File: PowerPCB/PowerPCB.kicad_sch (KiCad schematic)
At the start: 68 parts, among them J4 Conn_01x03, J5 Conn_01x02, J6 Conn_01x02, U1 TPS551892QWRYQRQ1, U2 FS1003-0600-AL, U4 TPS551892QWRYQRQ1

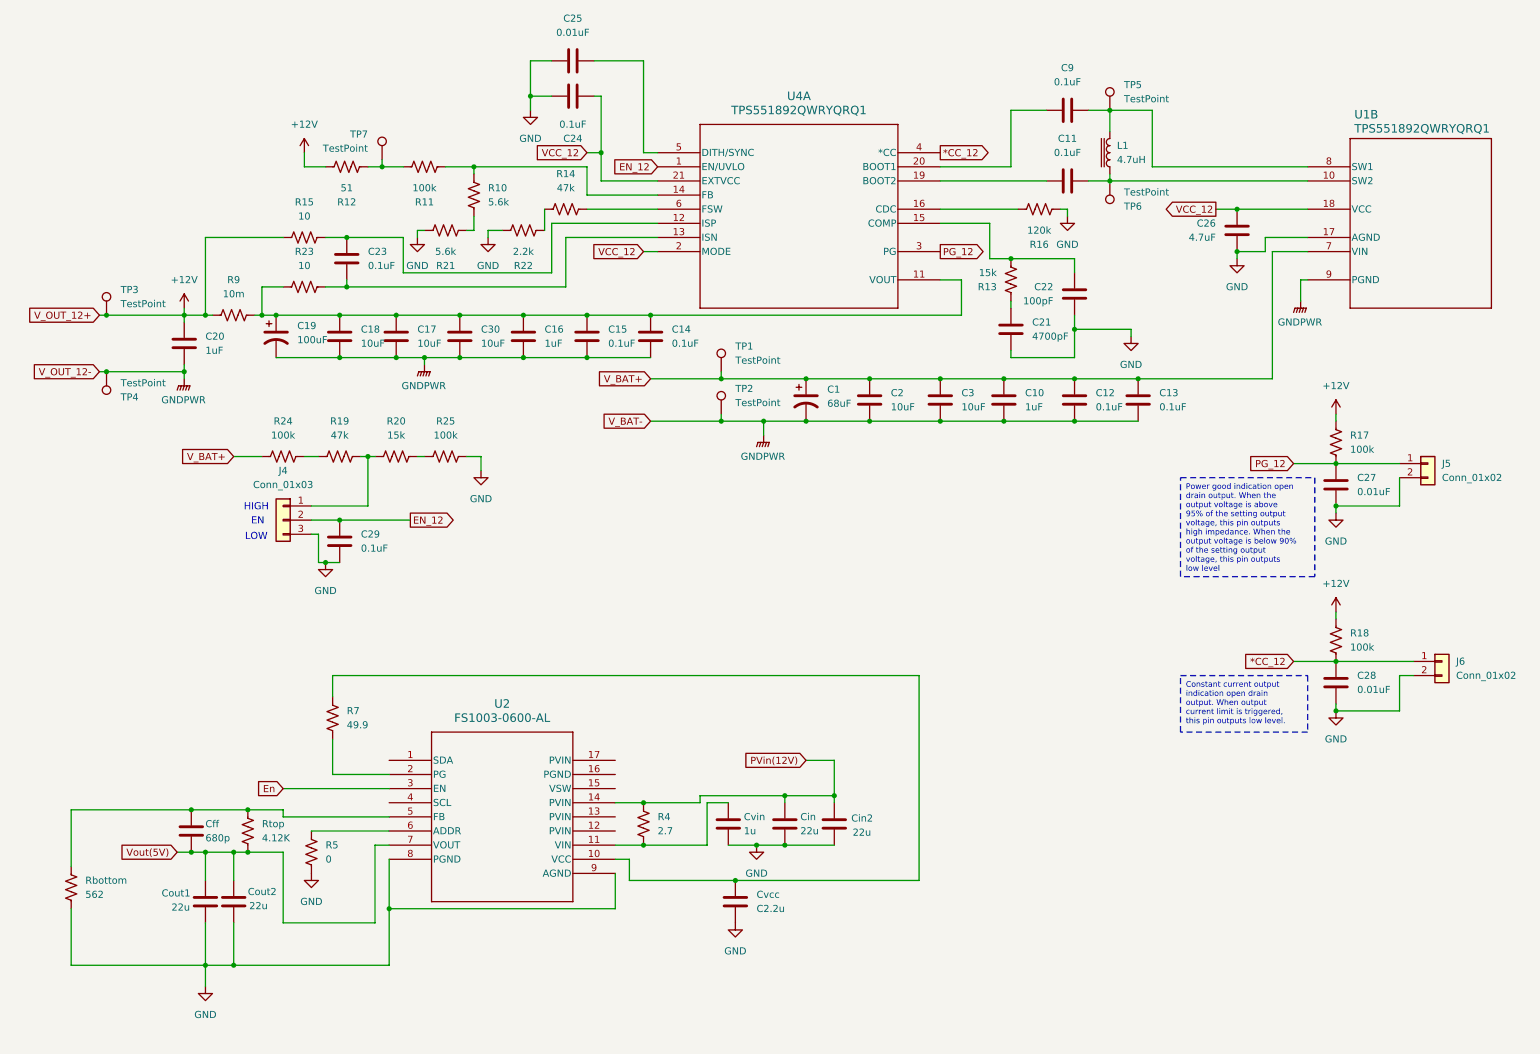
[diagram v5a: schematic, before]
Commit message: Change FS1003 to FS1403
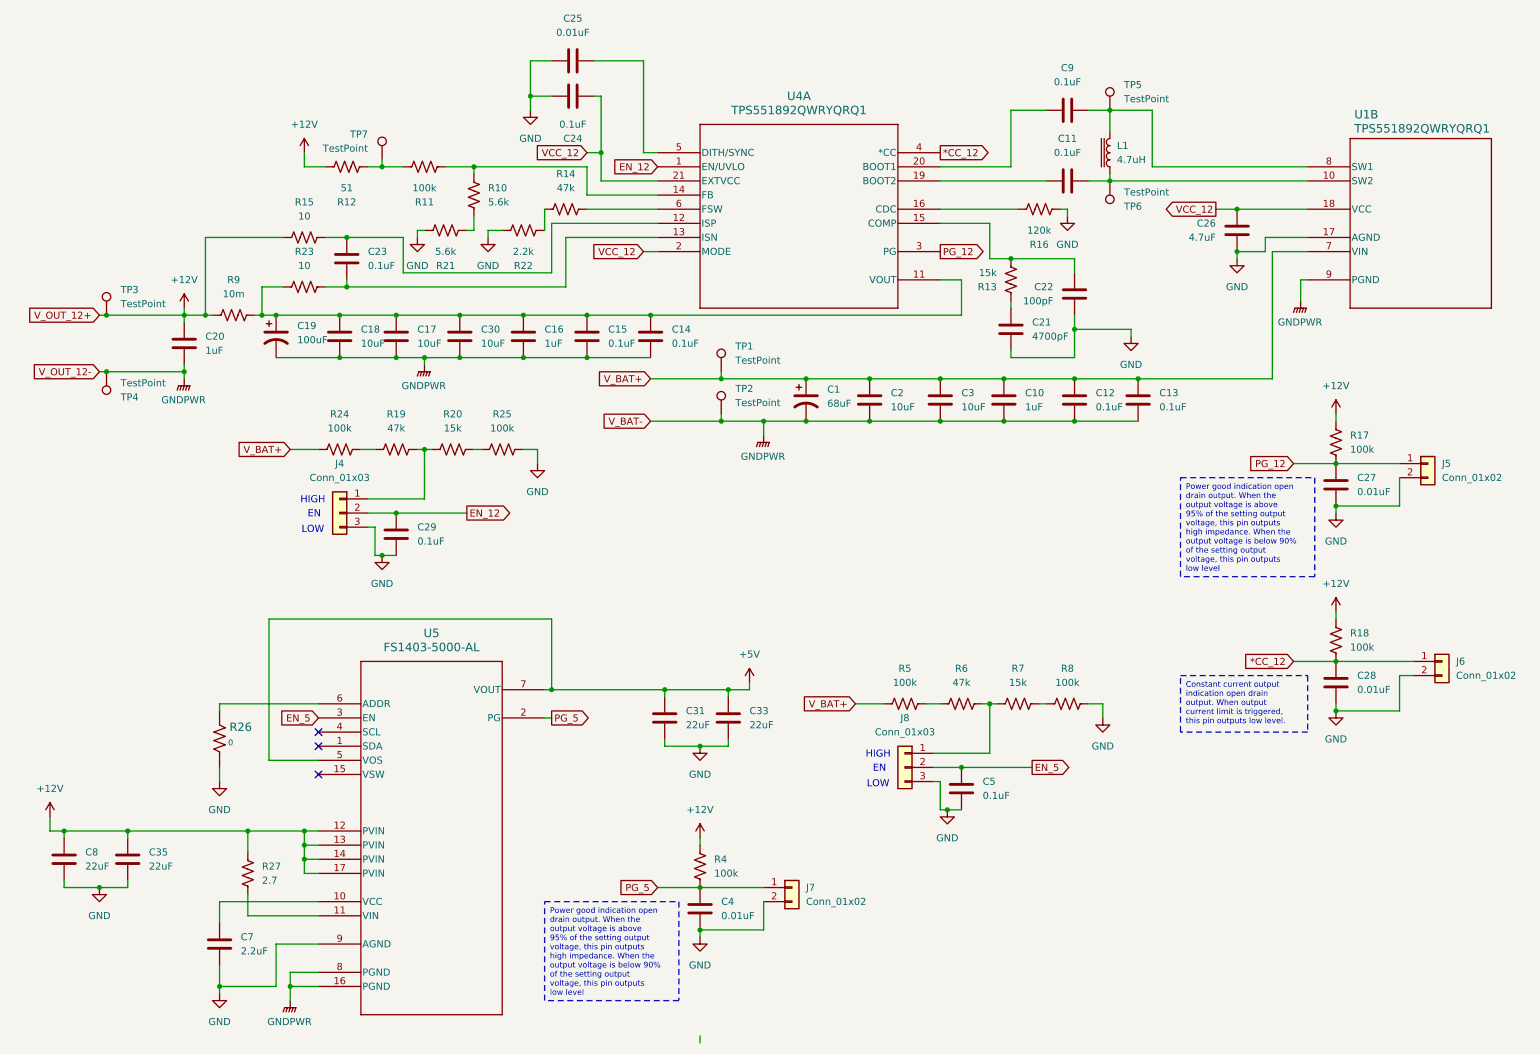
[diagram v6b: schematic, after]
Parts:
- removed Cff: 680p, symbol Device:C
- removed Cin, Cin2, Cout1, Cout2: 22u, symbol Device:C
- removed Cvcc: C2.2u, symbol Device:C
- removed Cvin: 1u, symbol Device:C
- removed Rbottom: 562, symbol Device:R_US
- removed Rtop: 4.12K, symbol Device:R_US
- removed U2: FS1003-0600-AL, Kicad_TitoSync_Footprints:fs1003-0600-al, symbol KiCad_TitoSync_Symbols:FS1003-0600-AL
- added C31, C33, C35, C8: 22uF, symbol Device:C
- added C4: 0.01uF, Capacitor_SMD:C_0805_2012Metric_Pad1.18x1.45mm_HandSolder, symbol Device:C
- added C5: 0.1uF, Capacitor_SMD:C_1206_3216Metric_Pad1.33x1.80mm_HandSolder, symbol Device:C
- added C7: 2.2uF, symbol Device:C
- added J7: Conn_01x02, Connector_PinHeader_2.54mm:PinHeader_1x02_P2.54mm_Vertical, symbol Connector_Generic:Conn_01x02
- added J8: Conn_01x03, Connector_PinHeader_2.54mm:PinHeader_1x03_P2.54mm_Vertical, symbol Connector_Generic:Conn_01x03
- added R26: 0, POWER STRIP DESIGN WITH ORIGINAL:0402, symbol POWER_STRIP_DESIGN_WITH_ORIGINAL-lib:R
- added R27: 2.7, symbol Device:R_US
- added R6: 47k, Resistor_SMD:R_0805_2012Metric_Pad1.20x1.40mm_HandSolder, symbol Device:R_US
- added R8: 100k, Resistor_SMD:R_0805_2012Metric_Pad1.20x1.40mm_HandSolder, symbol Device:R_US
- added U5: FS1403-5000-AL, Kicad_TitoSync_Footprints:FS1403_TDK, symbol KiCad_TitoSync_Symbols:FS1403-5000-AL
- R4: value 2.7 -> 100k; footprint (none) -> Resistor_SMD:R_0805_2012Metric_Pad1.20x1.40mm_HandSolder
- R5: value 0 -> 100k; footprint (none) -> Resistor_SMD:R_0805_2012Metric_Pad1.20x1.40mm_HandSolder
- R7: value 49.9 -> 15k; footprint (none) -> Resistor_SMD:R_0805_2012Metric_Pad1.20x1.40mm_HandSolder
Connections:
- net PVin(12V) is gone; now on net +12V: R4.1
- net +12V: now also C35.1, C8.1, R27.1, U5.12 (PVIN), U5.13 (PVIN), U5.14 (PVIN), U5.17 (PVIN)
- net GND: now also C31.2, C33.2, C35.2, C4.2, C5.2, C7.2, C8.2, J7.2 (Pin_2), J8.3 (Pin_3), R26.1, R8.2, U5.9 (AGND); no longer R5.2
- net GNDPWR: now also U5.16 (PGND), U5.8 (PGND)
- net V_BAT+: now also R5.1
- net PG_5: now reaches R4.2
- net PG_5: now also C4.1, J7.1 (Pin_1), U5.2 (PG)
- net at R7.1: now also J8.1 (Pin_1), R6.2
- net at R7.2: now also R8.1
- new net: R5.2, R6.1
- new net: R26.2, U5.6 (ADDR)
- new net: C7.1, U5.10 (VCC)
- new net: R27.2, U5.11 (VIN)
- new net +5V: C31.1, C33.1, U5.5 (VOS), U5.7 (VOUT)
- new net EN_5: C5.1, J8.2 (Pin_2), U5.3 (EN)
- no-connect marks 0 -> 3
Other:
- moved on the sheet: C29, J4, R19, R20, R24, R25

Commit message: Assign footprints
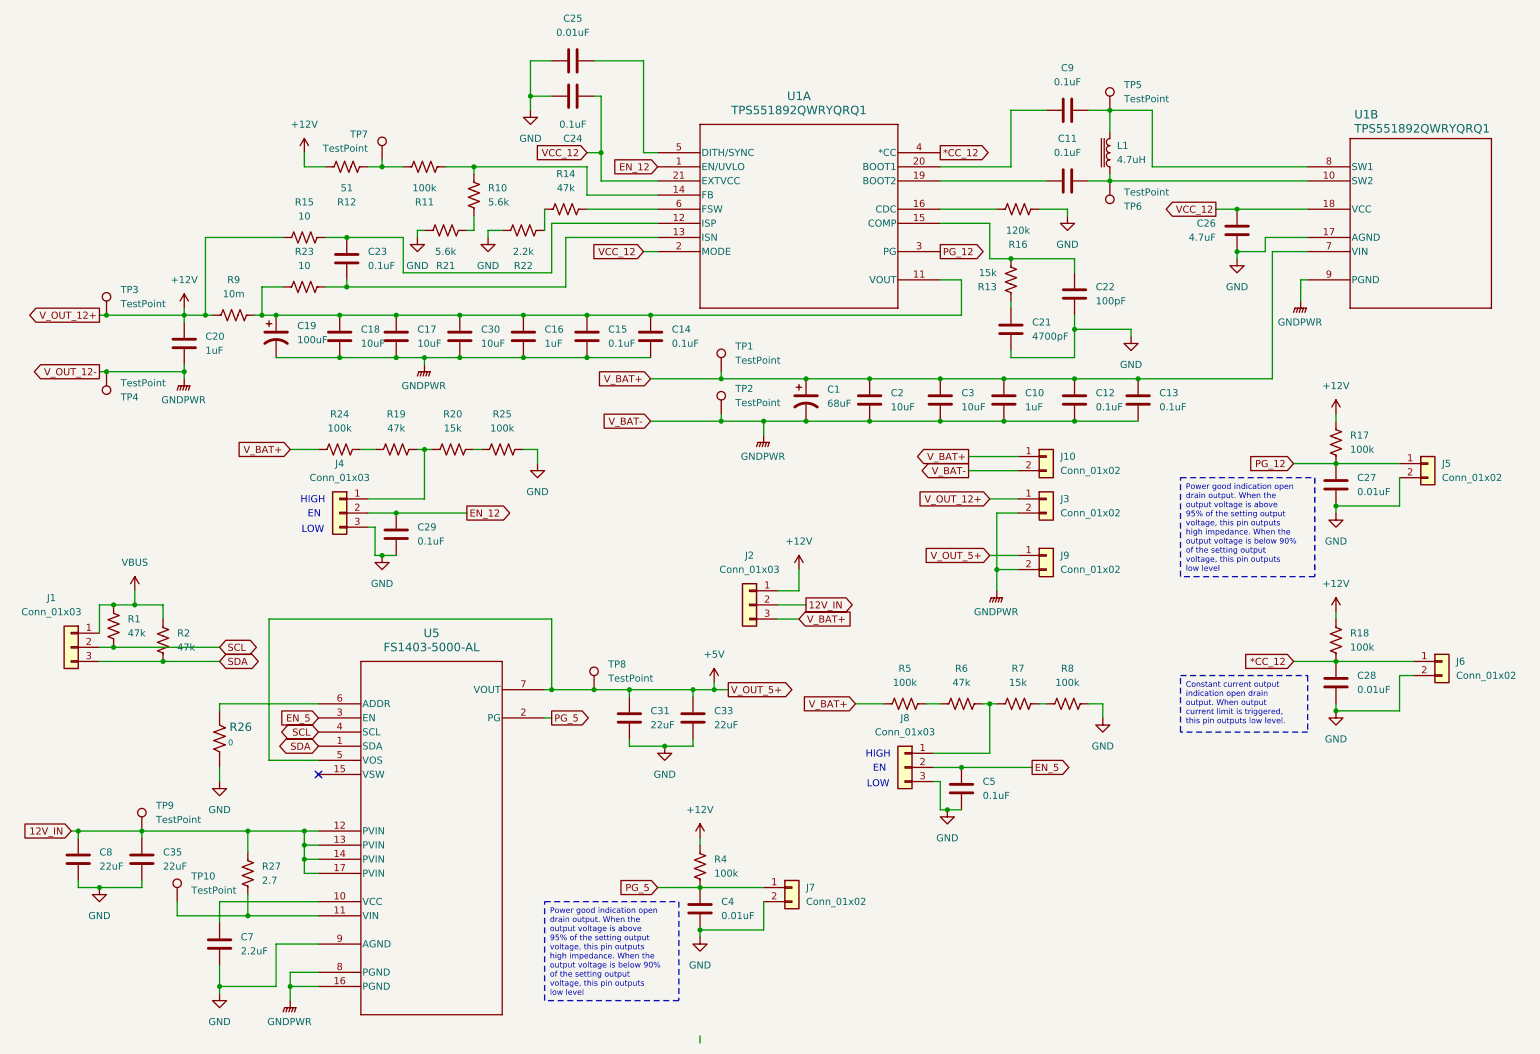
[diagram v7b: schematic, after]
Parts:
- added J1, J2: Conn_01x03, Connector_PinHeader_2.54mm:PinHeader_1x03_P2.54mm_Vertical, symbol Connector_Generic:Conn_01x03
- added J10, J3: Conn_01x02, TerminalBlock_4Ucon:TerminalBlock_4Ucon_1x02_P3.50mm_Horizontal, symbol Connector_Generic:Conn_01x02
- added J9: Conn_01x02, Connector_PinHeader_2.54mm:PinHeader_1x02_P2.54mm_Vertical, symbol Connector_Generic:Conn_01x02
- added R1, R2: 47k, Resistor_SMD:R_0805_2012Metric_Pad1.20x1.40mm_HandSolder, symbol Device:R_US
- added TP10, TP8, TP9: TestPoint, TestPoint:TestPoint_Keystone_5019_Miniature, symbol Connector:TestPoint
- C31, C33, C35, C7, C8: footprint (none) -> Capacitor_SMD:C_0805_2012Metric_Pad1.18x1.45mm_HandSolder
- J6: footprint Connector_PinHeader_2.54mm:PinHeader_1x02_P2.54mm_Vertical -> TerminalBlock_4Ucon:TerminalBlock_4Ucon_1x02_P3.50mm_Horizontal
- R26: footprint POWER STRIP DESIGN WITH ORIGINAL:0402 -> Resistor_SMD:R_0805_2012Metric_Pad1.20x1.40mm_HandSolder
- R27: footprint (none) -> Resistor_SMD:R_1210_3225Metric_Pad1.30x2.65mm_HandSolder
- TP1, TP2, TP3, TP4, TP5, TP6, TP7: footprint (none) -> TestPoint:TestPoint_Keystone_5019_Miniature
- renumbered U4 to U1
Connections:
- net +12V: now also J2.1 (Pin_1), J3.1 (Pin_1); no longer C35.1, C8.1, R27.1, U5.12 (PVIN), U5.13 (PVIN), U5.14 (PVIN), U5.17 (PVIN)
- net +5V: now also J9.1 (Pin_1), TP8.1
- net GNDPWR: now also J10.2 (Pin_2), J3.2 (Pin_2), J9.2 (Pin_2)
- net V_BAT+: now also J10.1 (Pin_1), J2.3 (Pin_3)
- net SDA: now reaches U5.1 (SDA)
- net SDA: now also J1.3 (Pin_3), R2.2
- net at R27.2, U5.11 (VIN): now also TP10.1
- net SCL: now reaches U5.4 (SCL)
- net SCL: now also J1.2 (Pin_2), R1.2
- new net 12V_IN: C35.1, C8.1, J2.2 (Pin_2), R27.1, TP9.1, U5.12 (PVIN), U5.13 (PVIN), U5.14 (PVIN), U5.17 (PVIN)
- new net VBUS: J1.1 (Pin_1), R1.1, R2.1
- no-connect marks 3 -> 1
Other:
- moved on the sheet: C31, C33, C35, C8, R16

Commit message: TPS551892 routed
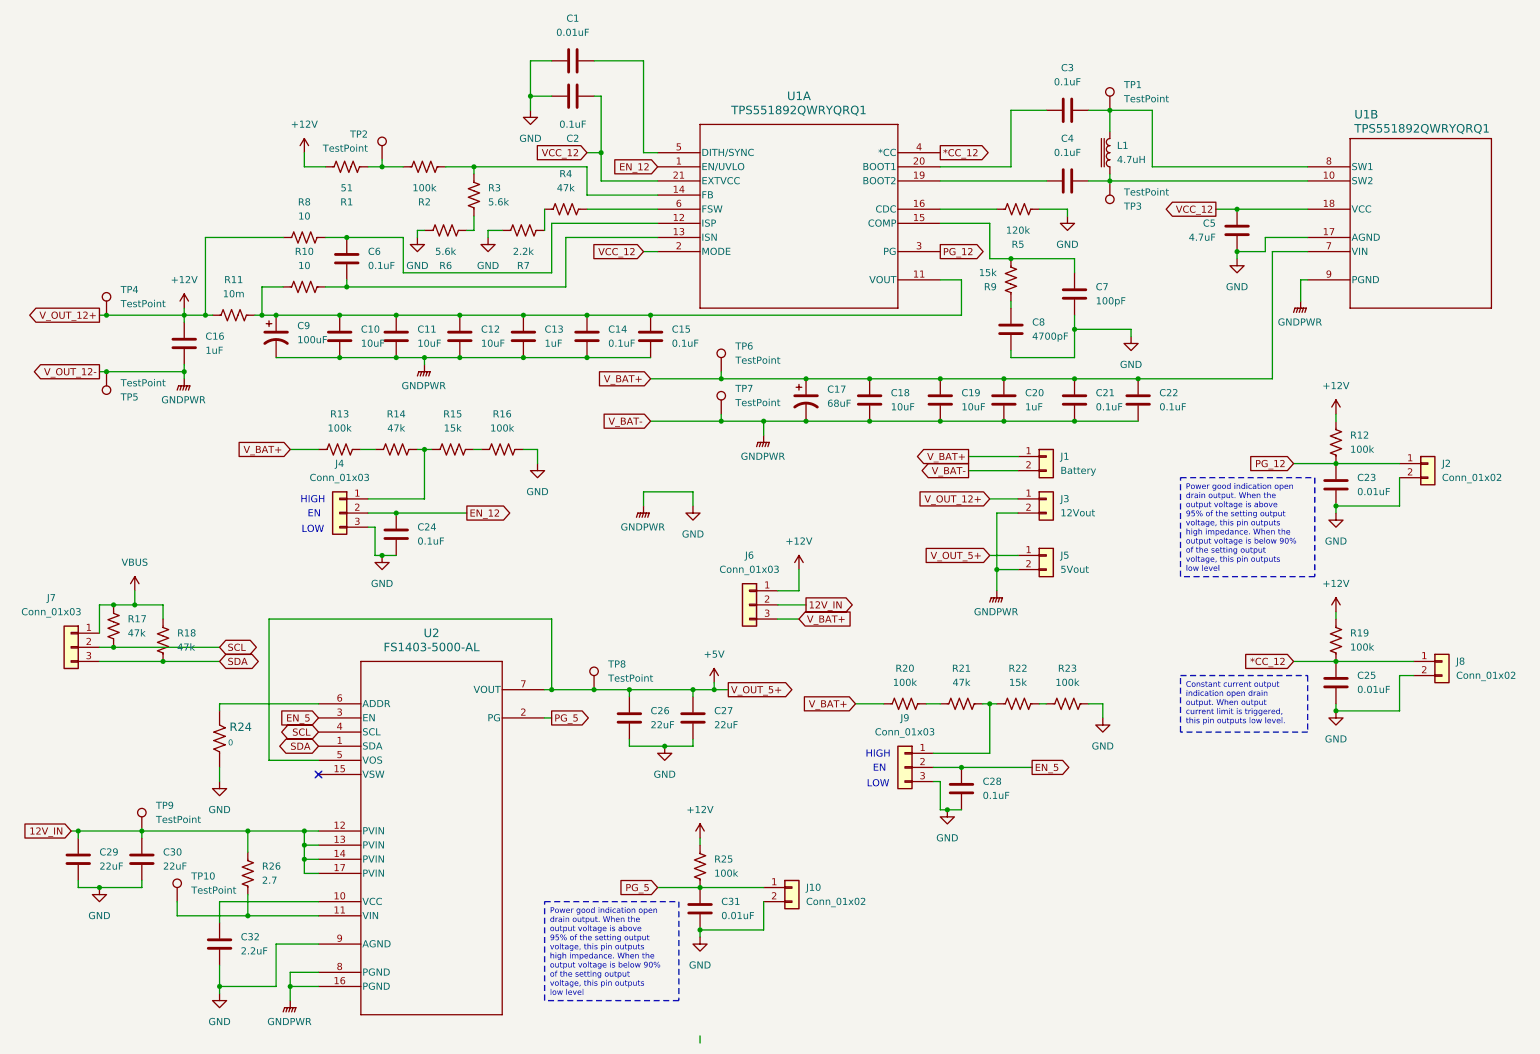
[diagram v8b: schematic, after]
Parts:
- J1: renamed from J10; value Conn_01x02 -> Battery
- J3: value Conn_01x02 -> 12Vout
- J5: renamed from J9; value Conn_01x02 -> 5Vout
- J8: renamed from J6; footprint TerminalBlock_4Ucon:TerminalBlock_4Ucon_1x02_P3.50mm_Horizontal -> Connector_PinHeader_2.54mm:PinHeader_1x02_P2.54mm_Vertical
- renumbered C25 to C1, C18 to C10, C17 to C11, C30 to C12, C16 to C13, C15 to C14, C14 to C15, C20 to C16, C1 to C17, C2 to C18, C3 to C19, C24 to C2, C10 to C20, C12 to C21, C13 to C22, C27 to C23, C29 to C24, C28 to C25, C31 to C26, C33 to C27, C5 to C28, C8 to C29, C9 to C3, C35 to C30, C4 to C31, C7 to C32, C11 to C4, C26 to C5, C23 to C6, C22 to C7, C21 to C8, C19 to C9, J7 to J10, J5 to J2, J2 to J6, J1 to J7, J8 to J9, R12 to R1, R23 to R10, R9 to R11, R17 to R12, R24 to R13, R19 to R14, R20 to R15, R25 to R16, R1 to R17, R2 to R18, R18 to R19, R11 to R2, R5 to R20, R6 to R21, R7 to R22, R8 to R23, R26 to R24, R4 to R25, R27 to R26, R10 to R3, R14 to R4, R16 to R5, R21 to R6, R22 to R7, R15 to R8, R13 to R9, TP5 to TP1, TP7 to TP2, TP6 to TP3, TP3 to TP4, TP4 to TP5, TP1 to TP6, TP2 to TP7, U5 to U2
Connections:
- net GNDPWR is gone; now on net GND: C10.2, C11.2, C12.2, C13.2, C14.2, C15.2, C16.2, C17.2, C18.2, C19.2, C20.2, C21.2, C22.2, C9.2, J1.2 (Pin_2), J3.2 (Pin_2), J5.2 (Pin_2), TP5.1, TP7.1, U1.9 (PGND), U2.16 (PGND), U2.8 (PGND)
